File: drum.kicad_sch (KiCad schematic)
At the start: 39 parts, among them J101 Cortex, J102 DX07S016JA3, SW101 SKSG, SW102 SKSG, U101 ATSAMD51J, U102 TPS78433QWDRBRQ1, Y101 32k768

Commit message: Replace diode
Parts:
- C107, C108: Manufacturer YAGEO -> TDK; Mouser 603-CC603JRNPO9BN180 -> 810-CGA3E2C0G1H180J; Product CC0603JRNPO9BN180 -> CGA3E2C0G1H180J080AA
- INFO102: value ~ -> (none)

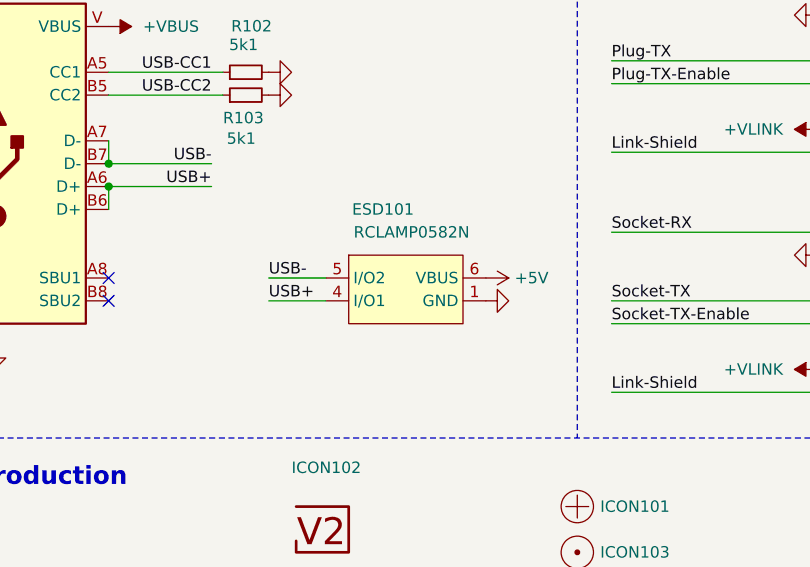
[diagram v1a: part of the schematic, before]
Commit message: Update ESD suppressor
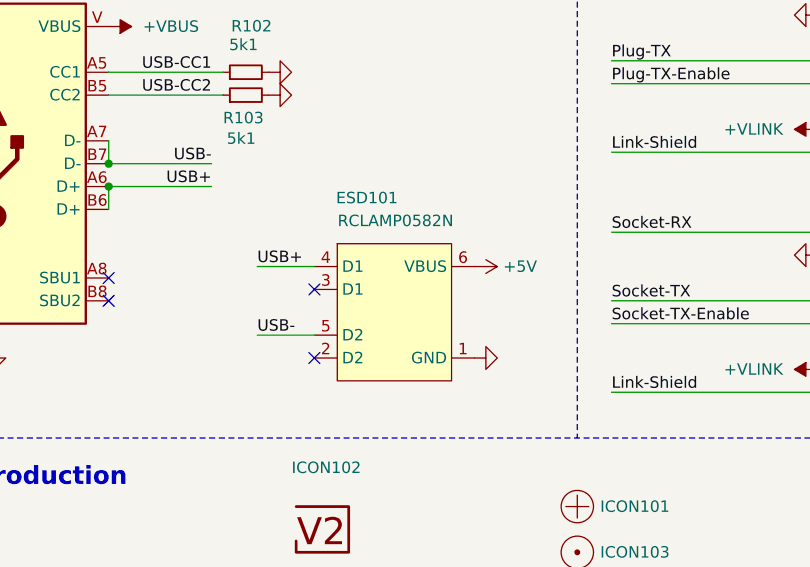
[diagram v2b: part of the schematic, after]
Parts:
- INFO102: value (none) -> ~
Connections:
- no-connect marks 26 -> 28
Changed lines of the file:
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@@
 	(title_block
 		(title "V2 drum")
-		(date "2026-03-11")
+		(date "2026-03-14")
 		(rev "2026-03-11")
 		(company "Versio Duo")
@@
 	)
 	(no_connect
+		(at 210.82 140.97)
+	)
+	(no_connect
 		(at 53.34 63.5)
 	)
@@
 	)
 	(no_connect
+		(at 210.82 148.59)
+	)
+	(no_connect
 		(at 193.04 92.71)
 	)
@@
 	(wire
 		(pts
-			(xy 205.74 142.24) (xy 212.09 142.24)
-		)
-		(stroke
-			(width 0)
-			(type default)
-		)
-	)
-	(wire
-		(pts
 			(xy 111.76 170.18) (xy 127 170.18)
 		)
@@
 	(wire
 		(pts
-			(xy 205.74 139.7) (xy 212.09 139.7)
+			(xy 204.47 146.05) (xy 210.82 146.05)
 		)
 		(stroke
@@
 	(wire
 		(pts
+			(xy 204.47 138.43) (xy 210.82 138.43)
+		)
+		(stroke
+			(width 0)
+			(type default)
+		)
+	)
+	(wire
+		(pts
 			(xy 267.97 50.8) (xy 281.94 50.8)
 		)
@@
 		)
 	)
+	(label "USB+"
+		(at 204.47 138.43 0)
+		(effects
+			(font
+				(size 1.27 1.27)
+			)
+			(justify left bottom)
+		)
+	)
 	(label "MISO"
 		(at 157.48 85.09 0)
@@
 	)
 	(label "USB-"
-		(at 205.74 139.7 0)
+		(at 204.47 146.05 0)
 		(effects
 			(font
@@
 		)
 	)
-	(label "USB+"
-		(at 205.74 142.24 0)
-		(effects
-			(font
-				(size 1.27 1.27)
-			)
-			(justify left bottom)
-		)
-	)
 	(label "Socket-TX"
 		(at 243.84 142.24 0)
@@
 	(symbol
 		(lib_id "V2_power:+5V")
-		(at 229.87 139.7 270)
+		(at 228.6 138.43 270)
 		(unit 1)
 		(exclude_from_sim no)
@@
 		(dnp no)
 		(property "Reference" "#PWR127"
-			(at 226.06 139.7 0)
+			(at 224.79 138.43 0)
 			(effects
 				(font
@@
 		)
 		(property "Value" "+5V"
-			(at 234.95 139.7 90)
+			(at 233.68 138.43 90)
 			(effects
 				(font
@@
 		)
 		(property "Footprint" ""
-			(at 229.87 139.7 0)
+			(at 228.6 138.43 0)
 			(effects
 				(font
@@
 		)
 		(property "Datasheet" ""
-			(at 229.87 139.7 0)
+			(at 228.6 138.43 0)
 			(effects
 				(font
@@
 		)
 		(property "Description" ""
-			(at 229.87 139.7 0)
+			(at 228.6 138.43 0)
 			(effects
 				(font
@@
 	(symbol
 		(lib_id "V2_ESD_Suppressor:RCLAMP0582N")
-		(at 220.98 139.7 0)
+		(at 219.71 143.51 0)
 		(unit 1)
 		(exclude_from_sim no)
@@
 		(dnp no)
 		(property "Reference" "ESD101"
-			(at 218.44 132.08 0)
+			(at 216.662 130.81 0)
 			(effects
 				(font
@@
 		)
 		(property "Value" "RCLAMP0582N"
-			(at 221.615 134.62 0)
+			(at 219.837 133.35 0)
 			(effects
 				(font
@@
 		)
 		(property "Footprint" "V2_ESD_Suppressor:SLP1210N6"
-			(at 220.98 154.94 0)
+			(at 219.71 158.75 0)
 			(effects
 				(font
@@
 		)
 		(property "Datasheet" ""
-			(at 220.98 139.7 0)
+			(at 219.71 143.51 0)
 			(effects
 				(font
@@
 		)
 		(property "Description" ""
-			(at 220.98 139.7 0)
+			(at 219.71 143.51 0)
 			(effects
 				(font
@@
 		)
 		(property "Mouser" "947-RCLAMP0582N.TCT"
-			(at 220.98 158.75 0)
+			(at 219.71 162.56 0)
 			(effects
 				(font
@@
 		)
 		(property "Product" "RCLAMP0582N.TCT"
-			(at 220.98 162.56 0)
+			(at 219.71 166.37 0)
 			(effects
 				(font
@@
 		)
 		(property "Manufacturer" "Semtech"
-			(at 220.98 160.02 0)
+			(at 219.71 163.83 0)
 			(effects
 				(font
@@
 	(symbol
 		(lib_id "V2_power:GND")
-		(at 229.87 142.24 90)
+		(at 228.6 148.59 90)
 		(unit 1)
 		(exclude_from_sim no)
@@
 		(dnp no)
 		(property "Reference" "#PWR128"
-			(at 236.22 142.24 0)
+			(at 234.95 148.59 0)
 			(effects
 				(font
@@
 		)
 		(property "Value" "GND"
-			(at 234.95 142.24 90)
+			(at 233.68 148.59 90)
 			(effects
 				(font
@@
 		)
 		(property "Footprint" ""
-			(at 229.87 142.24 0)
+			(at 228.6 148.59 0)
 			(effects
 				(font
@@
 		)
 		(property "Datasheet" ""
-			(at 229.87 142.24 0)
+			(at 228.6 148.59 0)
 			(effects
 				(font
@@
 		)
 		(property "Description" ""
-			(at 229.87 142.24 0)
+			(at 228.6 148.59 0)
 			(effects
 				(font
@@
 			)
 		)
-		(property "Value" ""
+		(property "Value" "~"
 			(at 248.92 182.88 0)
 			(effects

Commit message: Replace diode
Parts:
- INFO102: value ~ -> (none)

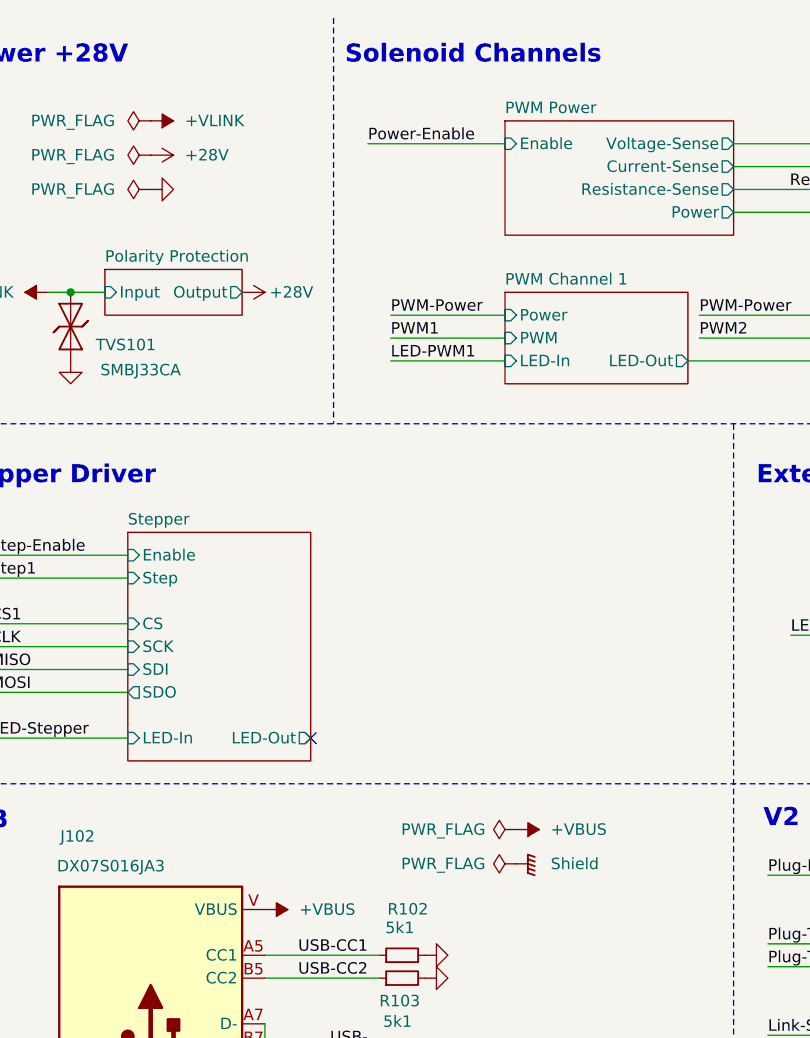
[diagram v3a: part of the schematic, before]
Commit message: Replace step-down
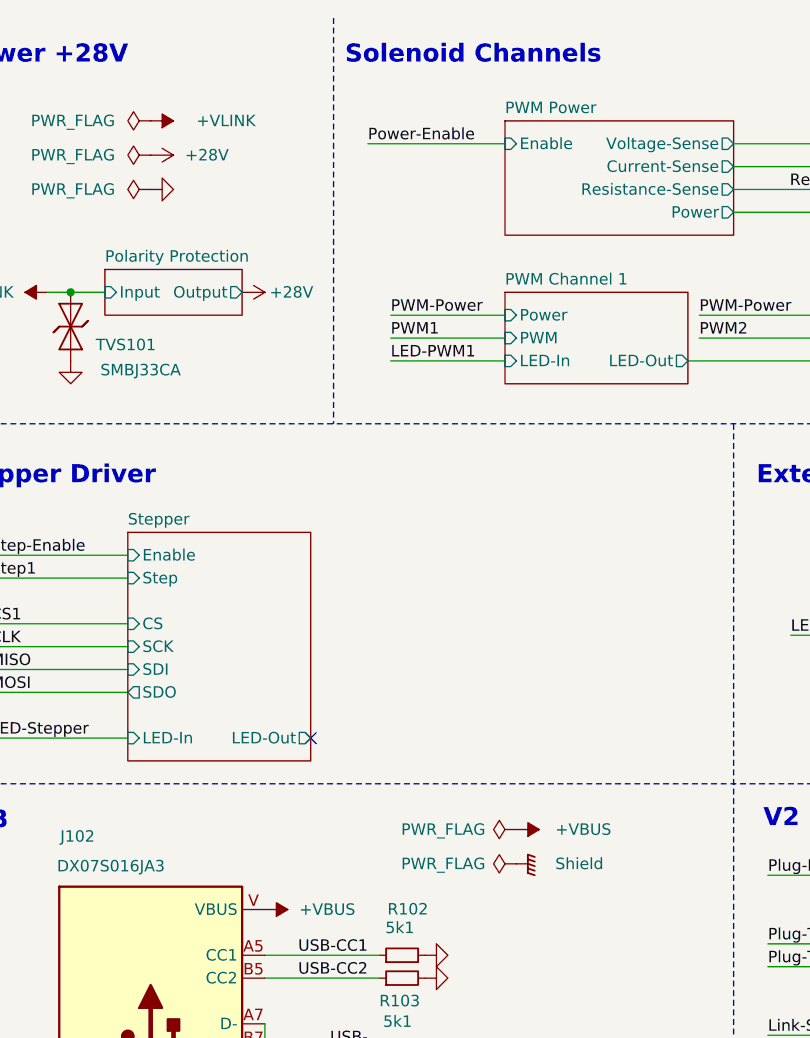
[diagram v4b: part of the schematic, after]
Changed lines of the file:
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@@
 		(in_pos_files yes)
 		(dnp no)
-		(fields_autoplaced yes)
 		(property "Reference" "#PWR116"
 			(at 212.09 102.87 0)
@@
 		)
 		(property "Value" "+VBUS"
-			(at 219.71 102.8699 90)
+			(at 220.218 102.8699 90)
 			(show_name no)
 			(do_not_autoplace no)
@@
 		(in_pos_files yes)
 		(dnp no)
-		(fields_autoplaced yes)
 		(property "Reference" "#PWR117"
 			(at 222.25 106.68 0)
@@
 		)
 		(property "Value" "Shield"
-			(at 219.71 106.6799 90)
+			(at 220.218 106.6799 90)
 			(show_name no)
 			(do_not_autoplace no)
@@
 		(in_pos_files yes)
 		(dnp no)
-		(fields_autoplaced yes)
 		(property "Reference" "#PWR102"
 			(at 162.56 24.13 0)
@@
 		)
 		(property "Value" "+VLINK"
-			(at 179.07 24.1299 90)
+			(at 180.34 24.1299 90)
 			(show_name no)
 			(do_not_autoplace no)

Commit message: Update
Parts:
- C101: renamed from C107; Id (none) -> Capacitor:${SYMBOL_NAME}; Rating (none) -> 50V
- C102: renamed from C108; Id (none) -> Capacitor:${SYMBOL_NAME}; Rating (none) -> 50V
- C103: renamed from C109; Id (none) -> Capacitor:${SYMBOL_NAME}
- C104: renamed from C110; Id (none) -> Capacitor:${SYMBOL_NAME}
- C105: renamed from C101; Id (none) -> Capacitor:${SYMBOL_NAME}
- C106: renamed from C102; Id (none) -> Capacitor:${SYMBOL_NAME}
- C107: renamed from C103; Id (none) -> Capacitor:${SYMBOL_NAME}
- C108: renamed from C104; Id (none) -> Capacitor:${SYMBOL_NAME}
- C109: renamed from C105; Id (none) -> Capacitor:${SYMBOL_NAME}
- C110: renamed from C106; Id (none) -> Capacitor:${SYMBOL_NAME}
- D101: renamed from D102; Id (none) -> LED:${SYMBOL_NAME}; Rating (none) -> 15mA
- D102: renamed from D103; Id (none) -> LED:${SYMBOL_NAME}; Rating (none) -> 15mA
- D103: renamed from D101; Id (none) -> LED:${SYMBOL_NAME}; Rating (none) -> 605nm
- ESD101: Id (none) -> ESD:${SYMBOL_NAME}; Rating (none) -> 20kV
- J102: Id (none) -> USB:${SYMBOL_NAME}; Rating (none) -> USB2.0
- R101: renamed from R104; Id (none) -> Resistor:${SYMBOL_NAME}
- R102: renamed from R101; Id (none) -> Resistor:${SYMBOL_NAME}
- R103: renamed from R102; Id (none) -> Resistor:${SYMBOL_NAME}
- R104: renamed from R103; Id (none) -> Resistor:${SYMBOL_NAME}
- SW101: renamed from SW102; Id (none) -> Button:${SYMBOL_NAME}; Rating (none) -> 1.6N
- SW102: renamed from SW101; Id (none) -> Button:${SYMBOL_NAME}; Rating (none) -> 1.6N
- TVS101: Id (none) -> Diode:${SYMBOL_NAME}
- U101: renamed from U102; Id (none) -> LDO:${SYMBOL_NAME}; Rating (none) -> 300mA
- U102: renamed from U101; Id (none) -> MCU:${SYMBOL_NAME}; Rating (none) -> Cortex-M4F
- Y101: Id (none) -> Crystal:${SYMBOL_NAME}; Rating (none) -> 10ppm
- renumbered ICON102 to ICON101, ICON101 to ICON102
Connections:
- net VDDCORE renamed +VCORE

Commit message: Good Bye Imperial
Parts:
- C101, C102: footprint V2_Capacitor_SMD:C_0603 -> V2_Capacitor_SMD:C_1608; symbol V2_Capacitor:0603_18p -> V2_Capacitor:1608_18p
- C103, C104: footprint V2_Capacitor_SMD:C_0805 -> V2_Capacitor_SMD:C_2012; symbol V2_Capacitor:0805_10u -> V2_Capacitor:2012_10u
- C105: footprint V2_Capacitor_SMD:C_0603 -> V2_Capacitor_SMD:C_1608; symbol V2_Capacitor:0603_10u -> V2_Capacitor:1608_10u
- C106, C107, C108, C109, C110: footprint V2_Capacitor_SMD:C_0603 -> V2_Capacitor_SMD:C_1608; symbol V2_Capacitor:0603_0u1 -> V2_Capacitor:1608_0u1
- D103: footprint V2_LED:LED_0603 -> V2_LED:LED_1608; symbol V2_LED:0603_Orange -> V2_LED:1608_Orange
- R101: footprint V2_Resistor_SMD:R_0603 -> V2_Resistor_SMD:R_1608; symbol V2_Resistor:0603_100k -> V2_Resistor:1608_100k
- R102: footprint V2_Resistor_SMD:R_0603 -> V2_Resistor_SMD:R_1608; symbol V2_Resistor:0603_330R -> V2_Resistor:1608_330R
- R103, R104: footprint V2_Resistor_SMD:R_0603 -> V2_Resistor_SMD:R_1608; symbol V2_Resistor:0603_5k1 -> V2_Resistor:1608_5k1
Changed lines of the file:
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@@
 	(title_block
 		(title "V2 drum")
-		(date "2026-04-14")
+		(date "2026-05-11")
 		(rev "2026-03-30")
 		(company "Versio Duo")
@@
 	)
 	(symbol
-		(lib_id "V2_Capacitor:0603_0u1")
+		(lib_id "V2_Capacitor:1608_0u1")
 		(at 109.22 24.13 0)
 		(unit 1)
@@
 			)
 		)
-		(property "Footprint" "V2_Capacitor_SMD:C_0603"
+		(property "Footprint" "V2_Capacitor_SMD:C_1608"
 			(at 109.22 41.148 0)
 			(hide yes)
@@
 		(unit 1)
 		(body_style 1)
-		(exclude_from_sim yes)
+		(exclude_from_sim no)
 		(in_bom no)
 		(on_board yes)
@@
 			)
 		)
+		(property "Sim.Enable" "0"
+			(at 240.03 170.18 0)
+			(hide yes)
+			(show_name no)
+			(do_not_autoplace no)
+			(effects
+				(font
+					(size 1.27 1.27)
+				)
+			)
+		)
 		(instances
 			(project "drum"
@@
 	)
 	(symbol
-		(lib_id "V2_LED:0603_Orange")
+		(lib_id "V2_LED:1608_Orange")
 		(at 129.54 86.36 0)
 		(mirror y)
@@
 			)
 		)
-		(property "Footprint" "V2_LED:LED_0603"
+		(property "Footprint" "V2_LED:LED_1608"
 			(at 129.54 86.36 90)
 			(hide yes)
@@
 			)
 		)
+		(property "Sim.Pins" "1=K 2=A"
+			(at 129.54 109.22 0)
+			(hide yes)
+			(show_name no)
+			(do_not_autoplace no)
+			(effects
+				(font
+					(size 1.27 1.27)
+				)
+			)
+		)
 		(pin "1"
 		)
@@
 	)
 	(symbol
-		(lib_id "V2_Resistor:0603_5k1")
+		(lib_id "V2_Resistor:1608_5k1")
 		(at 203.2 119.38 90)
 		(unit 1)
@@
 			)
 		)
-		(property "Footprint" "V2_Resistor_SMD:R_0603"
+		(property "Footprint" "V2_Resistor_SMD:R_1608"
 			(at 218.948 119.38 0)
 			(hide yes)
@@
 		(unit 1)
 		(body_style 1)
-		(exclude_from_sim yes)
+		(exclude_from_sim no)
 		(in_bom no)
 		(on_board yes)
@@
 			)
 		)
+		(property "Sim.Enable" "0"
+			(at 227.33 180.34 0)
+			(hide yes)
+			(show_name no)
+			(do_not_autoplace no)
+			(effects
+				(font
+					(size 1.27 1.27)
+				)
+			)
+		)
 		(instances
 			(project "drum"
@@
 	)
 	(symbol
-		(lib_id "V2_Capacitor:0805_10u")
+		(lib_id "V2_Capacitor:2012_10u")
 		(at 55.88 180.34 0)
 		(unit 1)
@@
 			)
 		)
-		(property "Footprint" "V2_Capacitor_SMD:C_0805"
+		(property "Footprint" "V2_Capacitor_SMD:C_2012"
 			(at 55.88 197.358 0)
 			(hide yes)
@@
 	)
 	(symbol
-		(lib_id "V2_Capacitor:0603_0u1")
+		(lib_id "V2_Capacitor:1608_0u1")
 		(at 119.38 24.13 0)
 		(unit 1)
@@
 			)
 		)
-		(property "Footprint" "V2_Capacitor_SMD:C_0603"
+		(property "Footprint" "V2_Capacitor_SMD:C_1608"
 			(at 119.38 41.148 0)
 			(hide yes)
@@
 		(unit 1)
 		(body_style 1)
-		(exclude_from_sim yes)
+		(exclude_from_sim no)
 		(in_bom no)
 		(on_board yes)
@@
 			)
 		)
+		(property "Sim.Enable" "0"
+			(at 240.03 165.1 0)
+			(hide yes)
+			(show_name no)
+			(do_not_autoplace no)
+			(effects
+				(font
+					(size 1.27 1.27)
+				)
+			)
+		)
 		(instances
 			(project "drum"
@@
 	)
 	(symbol
-		(lib_id "V2_Capacitor:0805_10u")
+		(lib_id "V2_Capacitor:2012_10u")
 		(at 30.48 180.34 0)
 		(unit 1)
@@
 			)
 		)
-		(property "Footprint" "V2_Capacitor_SMD:C_0805"
+		(property "Footprint" "V2_Capacitor_SMD:C_2012"
 			(at 30.48 197.358 0)
 			(hide yes)
@@
 	)
 	(symbol
-		(lib_id "V2_Capacitor:0603_18p")
+		(lib_id "V2_Capacitor:1608_18p")
 		(at 26.67 46.99 0)
 		(unit 1)
@@
 			)
 		)
-		(property "Footprint" "V2_Capacitor_SMD:C_0603"
+		(property "Footprint" "V2_Capacitor_SMD:C_1608"
 			(at 26.67 64.008 0)
 			(hide yes)
@@
 	)
 	(symbol
-		(lib_id "V2_Capacitor:0603_10u")
+		(lib_id "V2_Capacitor:1608_10u")
 		(at 57.15 24.13 0)
 		(unit 1)
@@
 			)
 		)
-		(property "Footprint" "V2_Capacitor_SMD:C_0603"
+		(property "Footprint" "V2_Capacitor_SMD:C_1608"
 			(at 57.15 41.148 0)
 			(hide yes)
@@
 	)
 	(symbol
-		(lib_id "V2_Capacitor:0603_18p")
+		(lib_id "V2_Capacitor:1608_18p")
 		(at 21.59 46.99 0)
 		(unit 1)
@@
 			)
 		)
-		(property "Footprint" "V2_Capacitor_SMD:C_0603"
+		(property "Footprint" "V2_Capacitor_SMD:C_1608"
 			(at 21.59 64.008 0)
 			(hide yes)
@@
 	)
 	(symbol
-		(lib_id "V2_Resistor:0603_330R")
+		(lib_id "V2_Resistor:1608_330R")
 		(at 138.43 86.36 90)
 		(unit 1)
@@
 			)
 		)
-		(property "Footprint" "V2_Resistor_SMD:R_0603"
+		(property "Footprint" "V2_Resistor_SMD:R_1608"
 			(at 154.178 86.36 0)
 			(hide yes)
@@
 	)
 	(symbol
-		(lib_id "V2_Capacitor:0603_0u1")
+		(lib_id "V2_Capacitor:1608_0u1")
 		(at 99.06 24.13 0)
 		(unit 1)
@@
 			)
 		)
-		(property "Footprint" "V2_Capacitor_SMD:C_0603"
+		(property "Footprint" "V2_Capacitor_SMD:C_1608"
 			(at 99.06 41.148 0)
 			(hide yes)
@@
 	)
 	(symbol
-		(lib_id "V2_Capacitor:0603_0u1")
+		(lib_id "V2_Capacitor:1608_0u1")
 		(at 78.74 24.13 0)
 		(unit 1)
@@
 			)
 		)
-		(property "Footprint" "V2_Capacitor_SMD:C_0603"
+		(property "Footprint" "V2_Capacitor_SMD:C_1608"
 			(at 78.74 41.148 0)
 			(hide yes)
@@
 	)
 	(symbol
-		(lib_id "V2_Resistor:0603_5k1")
+		(lib_id "V2_Resistor:1608_5k1")
 		(at 203.2 116.84 90)
 		(unit 1)
@@
 			)
 		)
-		(property "Footprint" "V2_Resistor_SMD:R_0603"
+		(property "Footprint" "V2_Resistor_SMD:R_1608"
 			(at 218.948 116.84 0)
 			(hide yes)
@@
 	)
 	(symbol
-		(lib_id "V2_Capacitor:0603_0u1")
+		(lib_id "V2_Capacitor:1608_0u1")
 		(at 88.9 24.13 0)
 		(unit 1)
@@
 			)
 		)
-		(property "Footprint" "V2_Capacitor_SMD:C_0603"
+		(property "Footprint" "V2_Capacitor_SMD:C_1608"
 			(at 88.9 41.148 0)
 			(hide yes)
@@
 	)
 	(symbol
-		(lib_id "V2_Resistor:0603_100k")
+		(lib_id "V2_Resistor:1608_100k")
 		(at 50.8 121.92 90)
 		(unit 1)
@@
 			)
 		)
-		(property "Footprint" "V2_Resistor_SMD:R_0603"
+		(property "Footprint" "V2_Resistor_SMD:R_1608"
 			(at 66.548 121.92 0)
 			(hide yes)
